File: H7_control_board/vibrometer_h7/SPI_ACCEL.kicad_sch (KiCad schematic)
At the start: 8 parts, among them J601 Conn_01x08_Socket, J602 Conn_01x08_Socket

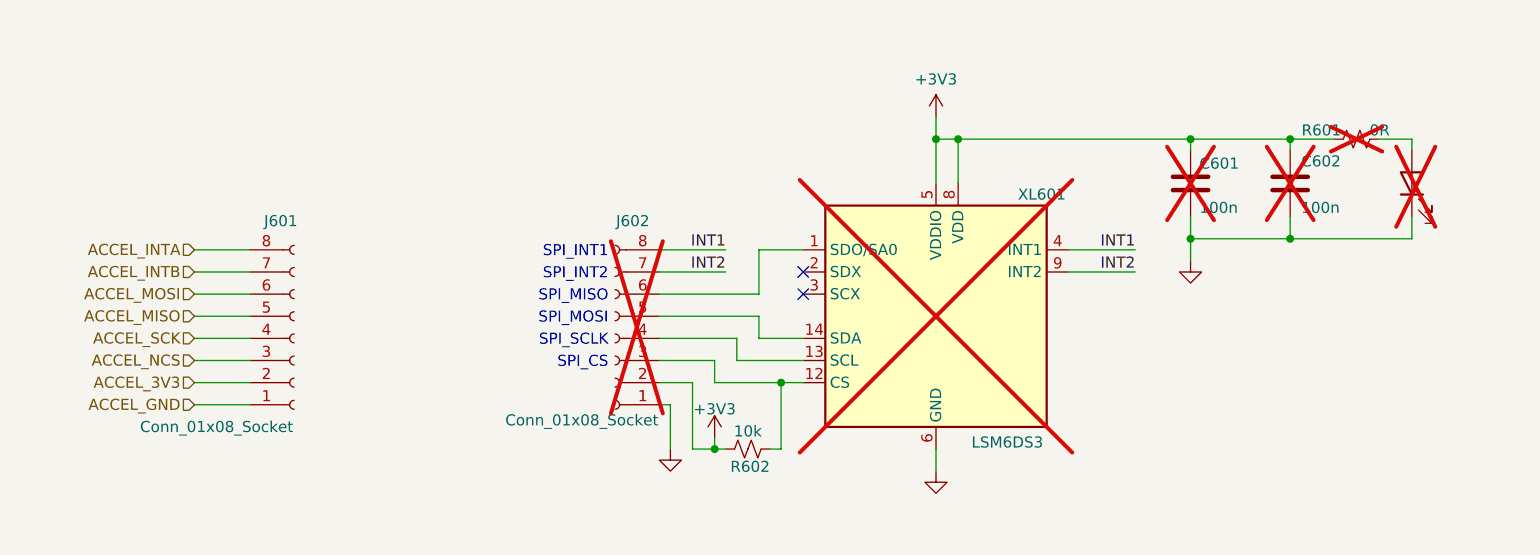
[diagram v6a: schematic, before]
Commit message: first pass at board routing
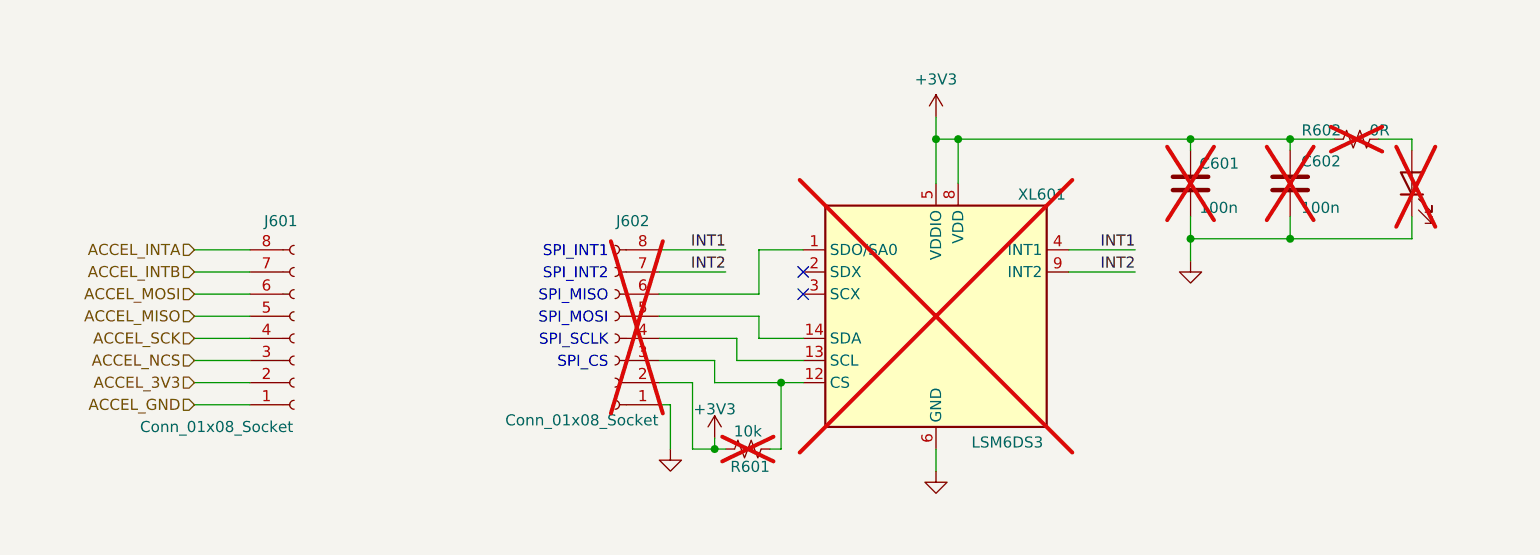
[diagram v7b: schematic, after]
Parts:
- C601, C602, D601, J602, XL601: now left out of the parts list
- J601: footprint (none) -> Connector_JST:JST_SH_SM08B-SRSS-TB_1x08-1MP_P1.00mm_Horizontal; LCSC (none) -> C160407
- R601: renamed from R602; footprint (none) -> Resistor_SMD:R_0603_1608Metric; LCSC (none) -> C25744; now not fitted; now left out of the parts list
- R602: renamed from R601; now left out of the parts list
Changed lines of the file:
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@@
 		(unit 1)
 		(exclude_from_sim no)
-		(in_bom yes)
-		(on_board yes)
+		(in_bom no)
+		(on_board no)
 		(dnp yes)
 		(property "Reference" "C602"
@@
 			)
 		)
-		(property "Footprint" ""
+		(property "Footprint" "Connector_JST:JST_SH_SM08B-SRSS-TB_1x08-1MP_P1.00mm_Horizontal"
 			(at 91.44 87.63 0)
 			(effects
@@
 			)
 		)
-		(property "Datasheet" "~"
+		(property "Datasheet" "https://www.lcsc.com/datasheet/lcsc_datasheet_2304140030_JST-SM08B-SRSS-TB-LF-SN_C160407.pdf"
 			(at 91.44 87.63 0)
 			(effects
@@
 			)
 		)
+		(property "LCSC" "C160407"
+			(at 91.44 87.63 0)
+			(effects
+				(font
+					(size 1.27 1.27)
+				)
+				(hide yes)
+			)
+		)
 		(pin "3"
 		)
@@
 		(unit 1)
 		(exclude_from_sim no)
-		(in_bom yes)
-		(on_board yes)
+		(in_bom no)
+		(on_board no)
 		(dnp yes)
 		(property "Reference" "C601"
@@
 		(unit 1)
 		(exclude_from_sim no)
-		(in_bom yes)
-		(on_board yes)
+		(in_bom no)
+		(on_board no)
 		(dnp yes)
 		(property "Reference" "XL601"
@@
 		(unit 1)
 		(exclude_from_sim no)
-		(in_bom yes)
-		(on_board yes)
+		(in_bom no)
+		(on_board no)
 		(dnp yes)
-		(property "Reference" "R601"
+		(property "Reference" "R602"
 			(at 211.582 63.754 90)
 			(effects
@@
 			(project "vibrometer_h7"
 				(path "/18de6987-156a-4b34-871e-cbbe1d261986/719d72ab-d813-461f-9482-52ce573716fd/4d0578b7-7312-4298-97a0-94006dea87de"
-					(reference "R601")
-					(unit 1)
-				)
-				(path "/18de6987-156a-4b34-871e-cbbe1d261986/719d72ab-d813-461f-9482-52ce573716fd/d33e5db2-c968-4012-a875-f240ab3119de"
-					(reference "R801")
-					(unit 1)
-				)
-				(path "/18de6987-156a-4b34-871e-cbbe1d261986/719d72ab-d813-461f-9482-52ce573716fd/e082b3de-4b18-4be4-ba81-d49e87b940c1"
-					(reference "R701")
+					(reference "R602")
+					(unit 1)
+				)
+				(path "/18de6987-156a-4b34-871e-cbbe1d261986/719d72ab-d813-461f-9482-52ce573716fd/d33e5db2-c968-4012-a875-f240ab3119de"
+					(reference "R802")
+					(unit 1)
+				)
+				(path "/18de6987-156a-4b34-871e-cbbe1d261986/719d72ab-d813-461f-9482-52ce573716fd/e082b3de-4b18-4be4-ba81-d49e87b940c1"
+					(reference "R702")
 					(unit 1)
 				)
@@
 		(unit 1)
 		(exclude_from_sim no)
-		(in_bom yes)
-		(on_board yes)
+		(in_bom no)
+		(on_board no)
 		(dnp yes)
 		(property "Reference" "J602"
@@
 		(unit 1)
 		(exclude_from_sim no)
-		(in_bom yes)
-		(on_board yes)
-		(dnp no)
-		(property "Reference" "R602"
+		(in_bom no)
+		(on_board no)
+		(dnp yes)
+		(property "Reference" "R601"
 			(at 143.764 102.362 90)
 			(effects
@@
 			)
 		)
-		(property "Footprint" ""
+		(property "Footprint" "Resistor_SMD:R_0603_1608Metric"
 			(at 143.51 100.33 0)
 			(effects
@@
 			)
 		)
-		(property "Datasheet" "~"
+		(property "Datasheet" "https://wmsc.lcsc.com/wmsc/upload/file/pdf/v2/lcsc/2206010100_UNI-ROYAL-Uniroyal-Elec-0402WGF1002TCE_C25744.pdf"
 			(at 143.51 100.33 0)
 			(effects
@@
 			)
 		)
-		(property "LCSC" ""
+		(property "LCSC" "C25744"
 			(at 143.51 100.33 0)
 			(effects
@@
 			(project "vibrometer_h7"
 				(path "/18de6987-156a-4b34-871e-cbbe1d261986/719d72ab-d813-461f-9482-52ce573716fd/4d0578b7-7312-4298-97a0-94006dea87de"
-					(reference "R602")
-					(unit 1)
-				)
-				(path "/18de6987-156a-4b34-871e-cbbe1d261986/719d72ab-d813-461f-9482-52ce573716fd/d33e5db2-c968-4012-a875-f240ab3119de"
-					(reference "R802")
-					(unit 1)
-				)
-				(path "/18de6987-156a-4b34-871e-cbbe1d261986/719d72ab-d813-461f-9482-52ce573716fd/e082b3de-4b18-4be4-ba81-d49e87b940c1"
-					(reference "R702")
+					(reference "R601")
+					(unit 1)
+				)
+				(path "/18de6987-156a-4b34-871e-cbbe1d261986/719d72ab-d813-461f-9482-52ce573716fd/d33e5db2-c968-4012-a875-f240ab3119de"
+					(reference "R801")
+					(unit 1)
+				)
+				(path "/18de6987-156a-4b34-871e-cbbe1d261986/719d72ab-d813-461f-9482-52ce573716fd/e082b3de-4b18-4be4-ba81-d49e87b940c1"
+					(reference "R701")
 					(unit 1)
 				)
@@
 		(unit 1)
 		(exclude_from_sim no)
-		(in_bom yes)
-		(on_board yes)
+		(in_bom no)
+		(on_board no)
 		(dnp yes)
 		(fields_autoplaced yes)

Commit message: lots of routing progress!!
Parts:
- renumbered R602 to R601, R601 to R602
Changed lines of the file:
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@@
 		(on_board no)
 		(dnp yes)
-		(property "Reference" "R602"
+		(property "Reference" "R601"
 			(at 211.582 63.754 90)
 			(effects
@@
 			(project "vibrometer_h7"
 				(path "/18de6987-156a-4b34-871e-cbbe1d261986/719d72ab-d813-461f-9482-52ce573716fd/4d0578b7-7312-4298-97a0-94006dea87de"
-					(reference "R602")
+					(reference "R601")
 					(unit 1)
 				)
 				(path "/18de6987-156a-4b34-871e-cbbe1d261986/719d72ab-d813-461f-9482-52ce573716fd/d33e5db2-c968-4012-a875-f240ab3119de"
-					(reference "R802")
+					(reference "R801")
 					(unit 1)
 				)
 				(path "/18de6987-156a-4b34-871e-cbbe1d261986/719d72ab-d813-461f-9482-52ce573716fd/e082b3de-4b18-4be4-ba81-d49e87b940c1"
-					(reference "R702")
+					(reference "R701")
 					(unit 1)
 				)
@@
 		(on_board no)
 		(dnp yes)
-		(property "Reference" "R601"
+		(property "Reference" "R602"
 			(at 143.764 102.362 90)
 			(effects
@@
 			(project "vibrometer_h7"
 				(path "/18de6987-156a-4b34-871e-cbbe1d261986/719d72ab-d813-461f-9482-52ce573716fd/4d0578b7-7312-4298-97a0-94006dea87de"
-					(reference "R601")
+					(reference "R602")
 					(unit 1)
 				)
 				(path "/18de6987-156a-4b34-871e-cbbe1d261986/719d72ab-d813-461f-9482-52ce573716fd/d33e5db2-c968-4012-a875-f240ab3119de"
-					(reference "R801")
+					(reference "R802")
 					(unit 1)
 				)
 				(path "/18de6987-156a-4b34-871e-cbbe1d261986/719d72ab-d813-461f-9482-52ce573716fd/e082b3de-4b18-4be4-ba81-d49e87b940c1"
-					(reference "R701")
-					(unit 1)
-				)
+					(reference "R702")
+					(unit 1)
+				)
